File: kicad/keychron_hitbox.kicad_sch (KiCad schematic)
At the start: 55 parts, among them U1 RP2040-Zero

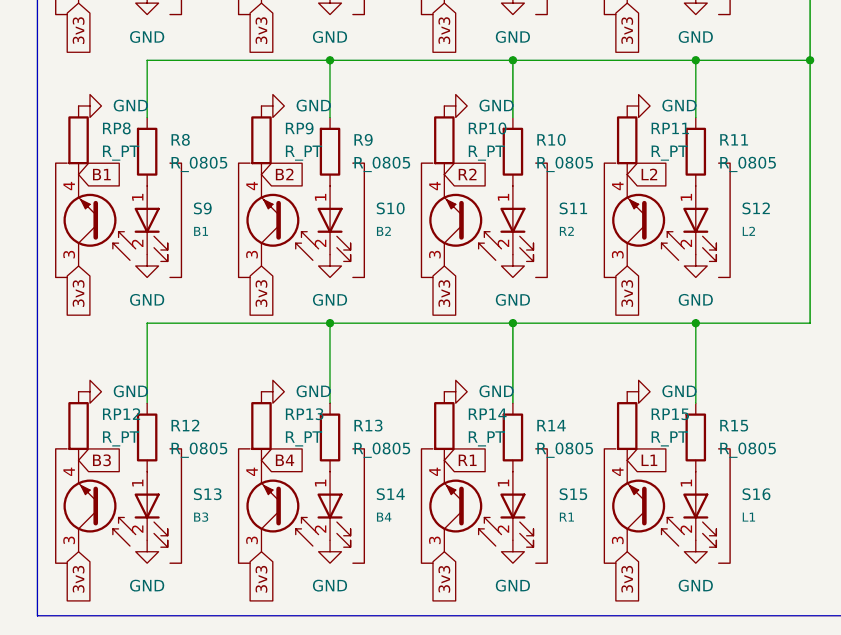
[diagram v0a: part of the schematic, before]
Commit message: updated seating for OLED & some acrylic designs
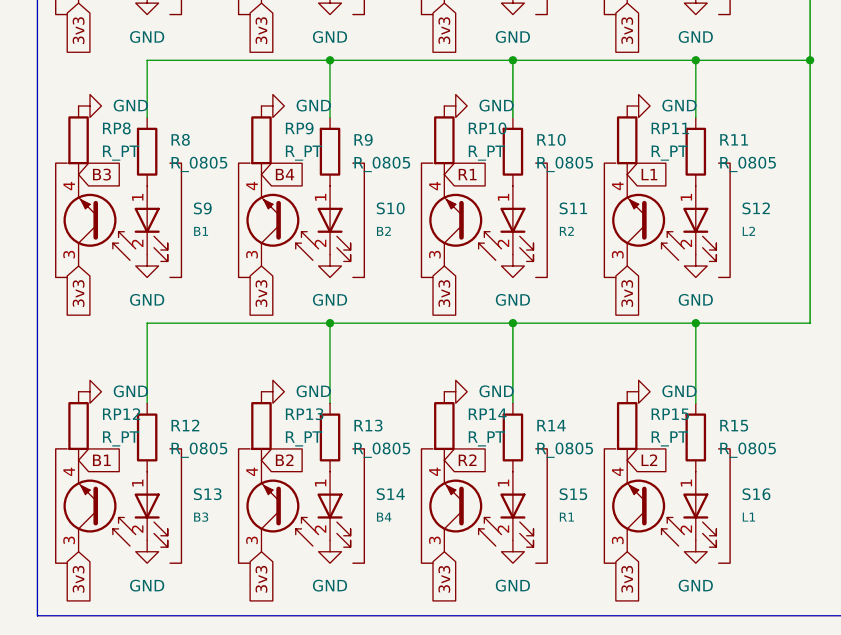
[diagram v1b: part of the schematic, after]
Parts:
- Brd1: footprint MyFootprints:128x64OLED -> MyFootprints:128x64OLED_hollowed
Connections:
- net B1: now also RP12.2, S13.4 (E); no longer RP8.2, S9.4 (E)
- net B2: now also RP13.2, S14.4 (E); no longer RP9.2, S10.4 (E)
- net B3: now also RP8.2, S9.4 (E); no longer RP12.2, S13.4 (E)
- net B4: now also RP9.2, S10.4 (E); no longer RP13.2, S14.4 (E)
- net L1: now also RP11.2, S12.4 (E); no longer RP15.2, S16.4 (E)
- net L2: now also RP15.2, S16.4 (E); no longer RP11.2, S12.4 (E)
- net R1: now also RP10.2, S11.4 (E); no longer RP14.2, S15.4 (E)
- net R2: now also RP14.2, S15.4 (E); no longer RP10.2, S11.4 (E)
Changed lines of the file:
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@@
 	(global_label "R2"
 		(shape input)
-		(at 77.47 91.44 0)
+		(at 77.47 123.19 0)
 		(fields_autoplaced yes)
 		(effects
@@
 		)
 		(property "Intersheetrefs" "${INTERSHEET_REFS}"
-			(at 82.9347 91.44 0)
+			(at 82.9347 123.19 0)
 			(effects
 				(font
@@
 	(global_label "L2"
 		(shape input)
-		(at 97.79 91.44 0)
+		(at 97.79 123.19 0)
 		(fields_autoplaced yes)
 		(effects
@@
 		)
 		(property "Intersheetrefs" "${INTERSHEET_REFS}"
-			(at 103.0128 91.44 0)
+			(at 103.0128 123.19 0)
 			(effects
 				(font
@@
 	(global_label "B4"
 		(shape input)
-		(at 57.15 123.19 0)
+		(at 57.15 91.44 0)
 		(fields_autoplaced yes)
 		(effects
@@
 		)
 		(property "Intersheetrefs" "${INTERSHEET_REFS}"
-			(at 62.6147 123.19 0)
+			(at 62.6147 91.44 0)
 			(effects
 				(font
@@
 	(global_label "L1"
 		(shape input)
-		(at 97.79 123.19 0)
+		(at 97.79 91.44 0)
 		(fields_autoplaced yes)
 		(effects
@@
 		)
 		(property "Intersheetrefs" "${INTERSHEET_REFS}"
-			(at 103.0128 123.19 0)
+			(at 103.0128 91.44 0)
 			(effects
 				(font
@@
 	(global_label "B1"
 		(shape input)
-		(at 36.83 91.44 0)
+		(at 36.83 123.19 0)
 		(fields_autoplaced yes)
 		(effects
@@
 		)
 		(property "Intersheetrefs" "${INTERSHEET_REFS}"
-			(at 42.2947 91.44 0)
+			(at 42.2947 123.19 0)
 			(effects
 				(font
@@
 	(global_label "B3"
 		(shape input)
-		(at 36.83 123.19 0)
+		(at 36.83 91.44 0)
 		(fields_autoplaced yes)
 		(effects
@@
 		)
 		(property "Intersheetrefs" "${INTERSHEET_REFS}"
-			(at 42.2947 123.19 0)
+			(at 42.2947 91.44 0)
 			(effects
 				(font
@@
 	(global_label "B2"
 		(shape input)
-		(at 57.15 91.44 0)
+		(at 57.15 123.19 0)
 		(fields_autoplaced yes)
 		(effects
@@
 		)
 		(property "Intersheetrefs" "${INTERSHEET_REFS}"
-			(at 62.6147 91.44 0)
+			(at 62.6147 123.19 0)
 			(effects
 				(font
@@
 	(global_label "R1"
 		(shape input)
-		(at 77.47 123.19 0)
+		(at 77.47 91.44 0)
 		(fields_autoplaced yes)
 		(effects
@@
 		)
 		(property "Intersheetrefs" "${INTERSHEET_REFS}"
-			(at 82.9347 123.19 0)
+			(at 82.9347 91.44 0)
 			(effects
 				(font
@@
 			)
 		)
-		(property "Footprint" "MyFootprints:128x64OLED"
+		(property "Footprint" "MyFootprints:128x64OLED_hollowed"
 			(at 204.47 95.25 0)
 			(effects

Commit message: adding version 1.1
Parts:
- removed U1: RP2040-Zero, RP2040-Zero:RP2040 Zero_flipped, symbol rp2040:RP2040-Zero
- added R16: R_0805, PCM_Resistor_SMD_AKL:R_0805_2012Metric, symbol PCM_Resistor_AKL:R_0805
- added RP16: R_PT, PCM_4ms_Resistor:R_0603, symbol MySymbols:R_PT
- added S1: S2, MyFootprints:Keychron_Optical_Switch_23mm, symbol MySymbols:OptSw
- added U1: ~, MyFootprints:6x6pushbutton, symbol MySymbols:4pin_pushbutton
- added U5: RP2040-Zero-extended, MyFootprints:RP2040 Zero zllpin, symbol MySymbols:RP2040-Zero-extended
- added U6: ~, MyFootprints:usba_header, symbol MySymbols:usba_in
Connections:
- net 3v3: now also S1.3 (C), U5.3 (3V3)
- net 5v: now also R16.1, U5.1 (5V), U6.1 (VCC)
- net A1: now also U5.9 (GP14)
- net A2: now also U1.2, U5.8 (GP15); no longer RP1.2, S2.4 (E)
- net B1: now also U5.16 (GP6)
- net B2: now also U5.17 (GP7)
- net B3: now also U5.22 (GP10)
- net B4: now also U5.21 (GP11)
- net DOWN: now also U5.13 (GP3)
- net GND: now also RP16.1, S1.2 (IR_K), U1.3, U5.2 (GND), U5.24 (GND), U6.4 (GND)
- net L1: now also U5.19 (GP13)
- net L2: now also U5.23 (GP9)
- net L3: now also U5.5 (GP28)
- net LEFT: now also U5.15 (GP5)
- net R1: now also U5.20 (GP12)
- net R2: now also U5.18 (GP8)
- net R3: now also U5.4 (GP29)
- net RIGHT: now also U5.14 (GP4)
- net S1: now also U5.10 (GP0)
- net S2: now also U5.11 (GP1)
- net SCL: now also U5.6 (GP27)
- net SDA: now also U5.7 (GP26)
- net UP: now also U5.12 (GP2)
- new net: R16.2, S1.1 (IR_A)
- new net D+: U5.28 (GP22), U6.3 (D+)
- new net D-: U5.27 (GP23), U6.2 (D-)
- new net E1: RP16.2, S1.4 (E), U5.25 (GP25)
- new net E2: RP1.2, S2.4 (E), U5.26 (GP24)
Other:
- note added: "USB"
- moved on the sheet: Brd1, U2, U3, U4
